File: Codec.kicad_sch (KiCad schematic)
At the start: 17 parts, among them U8 CS4272

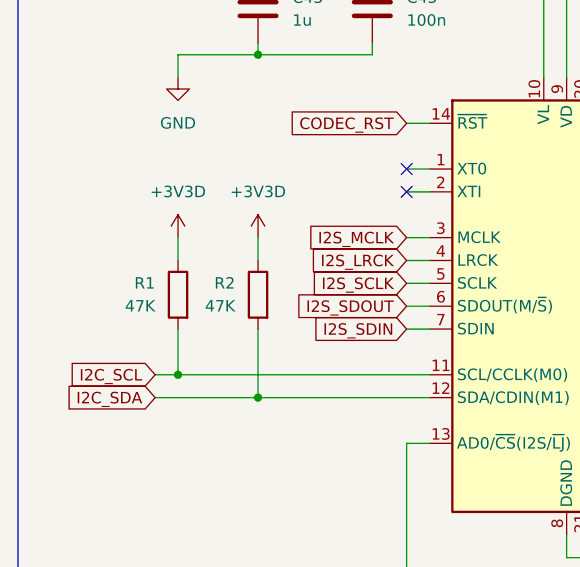
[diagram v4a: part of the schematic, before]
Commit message: RP2350 layout
Updated the layout for the RP2350.
Added board headers.
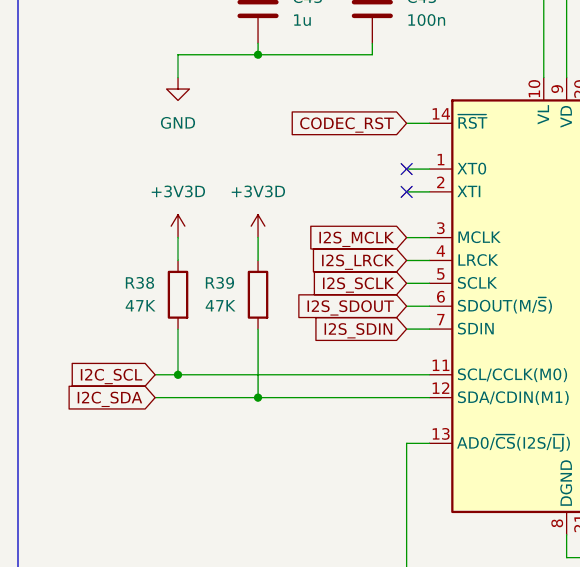
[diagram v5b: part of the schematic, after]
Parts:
- renumbered R1 to R38, R2 to R39
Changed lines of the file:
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@@
 		(dnp no)
 		(fields_autoplaced yes)
-		(property "Reference" "#PWR058"
+		(property "Reference" "#PWR059"
 			(at 102.87 53.34 0)
 			(effects
@@
 			(project "SimpleCodec"
 				(path "/4cbf131b-42e8-4a05-beea-68c6d66cdb1a/f7920eb9-f1f4-4882-8d74-32484732cce5"
-					(reference "#PWR058")
+					(reference "#PWR059")
 					(unit 1)
 				)
@@
 		(dnp no)
 		(fields_autoplaced yes)
-		(property "Reference" "#PWR02"
+		(property "Reference" "#PWR061"
 			(at 102.87 104.14 0)
 			(effects
@@
 			(project "SimpleCodec"
 				(path "/4cbf131b-42e8-4a05-beea-68c6d66cdb1a/f7920eb9-f1f4-4882-8d74-32484732cce5"
-					(reference "#PWR02")
+					(reference "#PWR061")
 					(unit 1)
 				)
@@
 		(dnp no)
 		(fields_autoplaced yes)
-		(property "Reference" "#PWR067"
+		(property "Reference" "#PWR069"
 			(at 187.96 88.9 0)
 			(effects
@@
 			(project "SimpleCodec"
 				(path "/4cbf131b-42e8-4a05-beea-68c6d66cdb1a/f7920eb9-f1f4-4882-8d74-32484732cce5"
-					(reference "#PWR067")
+					(reference "#PWR069")
 					(unit 1)
 				)
@@
 		(dnp no)
 		(fields_autoplaced yes)
-		(property "Reference" "#PWR059"
+		(property "Reference" "#PWR060"
 			(at 102.87 72.39 0)
 			(effects
@@
 			(project "SimpleCodec"
 				(path "/4cbf131b-42e8-4a05-beea-68c6d66cdb1a/f7920eb9-f1f4-4882-8d74-32484732cce5"
-					(reference "#PWR059")
+					(reference "#PWR060")
 					(unit 1)
 				)
@@
 		(dnp no)
 		(fields_autoplaced yes)
-		(property "Reference" "#PWR068"
+		(property "Reference" "#PWR070"
 			(at 187.96 116.84 0)
 			(effects
@@
 			(project "SimpleCodec"
 				(path "/4cbf131b-42e8-4a05-beea-68c6d66cdb1a/f7920eb9-f1f4-4882-8d74-32484732cce5"
-					(reference "#PWR068")
+					(reference "#PWR070")
 					(unit 1)
 				)
@@
 		(dnp no)
 		(fields_autoplaced yes)
-		(property "Reference" "#PWR063"
+		(property "Reference" "#PWR065"
 			(at 177.8 116.84 0)
 			(effects
@@
 			(project "SimpleCodec"
 				(path "/4cbf131b-42e8-4a05-beea-68c6d66cdb1a/f7920eb9-f1f4-4882-8d74-32484732cce5"
-					(reference "#PWR063")
+					(reference "#PWR065")
 					(unit 1)
 				)
@@
 		(dnp no)
 		(fields_autoplaced yes)
-		(property "Reference" "#PWR062"
+		(property "Reference" "#PWR064"
 			(at 165.1 144.78 0)
 			(effects
@@
 			(project "SimpleCodec"
 				(path "/4cbf131b-42e8-4a05-beea-68c6d66cdb1a/f7920eb9-f1f4-4882-8d74-32484732cce5"
-					(reference "#PWR062")
+					(reference "#PWR064")
 					(unit 1)
 				)
@@
 		(dnp no)
 		(fields_autoplaced yes)
-		(property "Reference" "#PWR064"
+		(property "Reference" "#PWR066"
 			(at 177.8 144.78 0)
 			(effects
@@
 			(project "SimpleCodec"
 				(path "/4cbf131b-42e8-4a05-beea-68c6d66cdb1a/f7920eb9-f1f4-4882-8d74-32484732cce5"
-					(reference "#PWR064")
+					(reference "#PWR066")
 					(unit 1)
 				)
@@
 		(dnp no)
 		(fields_autoplaced yes)
-		(property "Reference" "#PWR061"
+		(property "Reference" "#PWR063"
 			(at 139.7 144.78 0)
 			(effects
@@
 			(project "SimpleCodec"
 				(path "/4cbf131b-42e8-4a05-beea-68c6d66cdb1a/f7920eb9-f1f4-4882-8d74-32484732cce5"
-					(reference "#PWR061")
+					(reference "#PWR063")
 					(unit 1)
 				)
@@
 		(dnp no)
 		(fields_autoplaced yes)
-		(property "Reference" "#PWR065"
+		(property "Reference" "#PWR067"
 			(at 179.07 53.34 0)
 			(effects
@@
 			(project "SimpleCodec"
 				(path "/4cbf131b-42e8-4a05-beea-68c6d66cdb1a/f7920eb9-f1f4-4882-8d74-32484732cce5"
-					(reference "#PWR065")
+					(reference "#PWR067")
 					(unit 1)
 				)
@@
 		(dnp no)
 		(fields_autoplaced yes)
-		(property "Reference" "#PWR060"
+		(property "Reference" "#PWR062"
 			(at 119.38 144.78 0)
 			(effects
@@
 			(project "SimpleCodec"
 				(path "/4cbf131b-42e8-4a05-beea-68c6d66cdb1a/f7920eb9-f1f4-4882-8d74-32484732cce5"
-					(reference "#PWR060")
+					(reference "#PWR062")
 					(unit 1)
 				)
@@
 		(dnp no)
 		(fields_autoplaced yes)
-		(property "Reference" "#PWR066"
+		(property "Reference" "#PWR068"
 			(at 187.96 69.85 0)
 			(effects
@@
 			(project "SimpleCodec"
 				(path "/4cbf131b-42e8-4a05-beea-68c6d66cdb1a/f7920eb9-f1f4-4882-8d74-32484732cce5"
-					(reference "#PWR066")
+					(reference "#PWR068")
 					(unit 1)
 				)
@@
 		(on_board yes)
 		(dnp no)
-		(property "Reference" "R2"
+		(property "Reference" "R39"
 			(at 100.33 105.4099 0)
 			(effects
@@
 			(project "SimpleCodec"
 				(path "/4cbf131b-42e8-4a05-beea-68c6d66cdb1a/f7920eb9-f1f4-4882-8d74-32484732cce5"
-					(reference "R2")
+					(reference "R39")
 					(unit 1)
 				)
@@
 		(on_board yes)
 		(dnp no)
-		(property "Reference" "R1"
+		(property "Reference" "R38"
 			(at 91.44 105.4099 0)
 			(effects
@@
 			(project "SimpleCodec"
 				(path "/4cbf131b-42e8-4a05-beea-68c6d66cdb1a/f7920eb9-f1f4-4882-8d74-32484732cce5"
-					(reference "R1")
+					(reference "R38")
 					(unit 1)
 				)
@@
 		(dnp no)
 		(fields_autoplaced yes)
-		(property "Reference" "#PWR01"
+		(property "Reference" "#PWR058"
 			(at 93.98 104.14 0)
 			(effects
@@
 			(project "SimpleCodec"
 				(path "/4cbf131b-42e8-4a05-beea-68c6d66cdb1a/f7920eb9-f1f4-4882-8d74-32484732cce5"
-					(reference "#PWR01")
-					(unit 1)
-				)
+					(reference "#PWR058")
+					(unit 1)
+				)
